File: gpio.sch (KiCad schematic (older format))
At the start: 1 part, among them U1 LFE5U-85F-6BG381C

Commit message: GPDI routed
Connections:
- net LTDC_TO_FPGA_B5: now also U1.B3 (PL14D); no longer U1.E5 (PL20C)
- net LTDC_TO_FPGA_B6: now also U1.F5 (PL20D); no longer U1.B2 (VREF1_7)
- net LTDC_TO_FPGA_B7: now also U1.E5 (PL20C); no longer U1.C2 (PL35D)
- net LTDC_TO_FPGA_G2: now also U1.B2 (VREF1_7); no longer U1.B3 (PL14D)
- net LTDC_TO_FPGA_R6: now also U1.C2 (PL35D); no longer U1.F5 (PL20D)
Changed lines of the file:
@@
 Text GLabel 4200 4000 0    60   Input ~ 0
 LTDC_TO_FPGA_R5
-Text GLabel 5700 4200 2    60   Input ~ 0
+Text GLabel 5700 4400 2    60   Input ~ 0
 LTDC_TO_FPGA_R6
 Text GLabel 4200 4900 0    60   Input ~ 0
@@
 Text GLabel 5700 5000 2    60   Input ~ 0
 LTDC_TO_FPGA_G6
-Text GLabel 5700 4400 2    60   Input ~ 0
+Text GLabel 4200 4200 0    60   Input ~ 0
 LTDC_TO_FPGA_B7
-Text GLabel 4200 4400 0    60   Input ~ 0
+Text GLabel 5700 4200 2    60   Input ~ 0
 LTDC_TO_FPGA_B6
-Text GLabel 4200 4200 0    60   Input ~ 0
+Text GLabel 5700 3800 2    60   Input ~ 0
 LTDC_TO_FPGA_B5
 Text GLabel 4200 4300 0    60   Input ~ 0
@@
 Text GLabel 5700 4600 2    60   Input ~ 0
 LTDC_TO_FPGA_B3
-Text GLabel 5700 3800 2    60   Input ~ 0
+Text GLabel 4200 4400 0    60   Input ~ 0
 LTDC_TO_FPGA_G2
 Text GLabel 5700 4900 2    60   Input ~ 0

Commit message: Adding DIB_V2 connector for SERDES, change battery, initial power fixes power
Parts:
- added J1: Conn_02x08_Odd_Even, Connector_PinSocket_2.54mm:PinSocket_2x08_P2.54mm_Horizontal, symbol Connector_Generic:Conn_02x08_Odd_Even
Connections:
- net labels added: +1V1, +2V5, +3V3, GND, S_0_N, S_0_P, S_1_N, S_1_P, S_2_N, S_2_P, S_3_N, S_3_P, S_C_N, S_C_P
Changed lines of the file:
@@
 EESchema Schematic File Version 4
-EELAYER 30 0
+LIBS:ulx3s-cache
+EELAYER 29 0
 EELAYER END
 $Descr A4 11693 8268
@@
 Text GLabel 5700 2200 2    60   Input ~ 0
 LTDC_FROM_FPGA_R4
+$Comp
+L Connector_Generic:Conn_02x08_Odd_Even J1
+U 1 1 61FF604B
+P 8450 3700
+F 0 "J1" H 8500 3075 50  0000 C CNN
+F 1 "Conn_02x08_Odd_Even" H 8500 3166 50  0000 C CNN
+F 2 "Connector_PinSocket_2.54mm:PinSocket_2x08_P2.54mm_Horizontal" H 8450 3700 50  0001 C CNN
+F 3 "~" H 8450 3700 50  0001 C CNN
+	1    8450 3700
+	-1   0    0    1
+$EndComp
+Text GLabel 8150 3300 0    60   Input ~ 0
++3V3
+Text GLabel 8150 3400 0    60   Input ~ 0
++2V5
+Text GLabel 8150 3500 0    60   Input ~ 0
++1V1
+Text GLabel 8650 3300 2    60   Input ~ 0
+GND
+Text GLabel 8650 3400 2    60   Input ~ 0
+GND
+Text GLabel 8650 3500 2    60   Input ~ 0
+GND
+Text GLabel 8150 3800 0    60   Input ~ 0
+S_0_P
+Text GLabel 8150 3900 0    60   Input ~ 0
+S_0_N
+Text GLabel 8150 3600 0    60   Input ~ 0
+S_C_P
+Text GLabel 8150 3700 0    60   Input ~ 0
+S_C_N
+Text GLabel 8150 4000 0    60   Input ~ 0
+S_1_P
+Text GLabel 8650 4000 2    60   Input ~ 0
+S_1_N
+Text GLabel 8650 3600 2    60   Input ~ 0
+S_2_P
+Text GLabel 8650 3700 2    60   Input ~ 0
+S_2_N
+Text GLabel 8650 3800 2    60   Input ~ 0
+S_3_P
+Text GLabel 8650 3900 2    60   Input ~ 0
+S_3_N
 $EndSCHEMATC

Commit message: Routing long signals
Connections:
- net labels added: SPI2_TO_FPGA_CLK, SPI2_TO_FPGA_CSB, SPI2_TO_FPGA_IRQ
- net labels removed: FREE10, FREE5, FREE_LEFT_10, SPI5_FROM_FPGA_CLK
- no-connect marks 22 -> 19
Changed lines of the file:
@@
 Text GLabel 4200 1900 0    50   BiDi ~ 0
 SPI4_TO_FPGA_CLK
-Text GLabel 4200 3900 0    60   Input ~ 0
-FREE_LEFT_10
-Text GLabel 5700 5100 2    60   Input ~ 0
-FREE10
 Text GLabel 5700 4100 2    60   Input ~ 0
 FREE8
-Text GLabel 5700 3900 2    60   Input ~ 0
-FREE5
 Text GLabel 5700 3600 2    60   Input ~ 0
 FREE6
-Text GLabel 5700 2000 2    50   BiDi ~ 0
-SPI5_FROM_FPGA_CLK
 Text GLabel 5700 1900 2    50   BiDi ~ 0
 SPI4_FROM_FPGA_CLK
@@
 NoConn ~ 5700 2300
 NoConn ~ 5700 2100
-NoConn ~ 4200 3900
-NoConn ~ 5700 5100
 NoConn ~ 5700 4100
-NoConn ~ 5700 3900
 NoConn ~ 5700 3600
 Text GLabel 5700 2200 2    60   Input ~ 0
@@
 Text GLabel 8650 3900 2    60   Input ~ 0
 S_3_N
+Text GLabel 5700 5100 2    50   BiDi ~ 0
+SPI2_TO_FPGA_CLK
+Text GLabel 5700 3900 2    50   BiDi ~ 0
+SPI2_TO_FPGA_IRQ
+Text GLabel 4200 3900 0    50   BiDi ~ 0
+SPI2_TO_FPGA_CSB
 $EndSCHEMATC

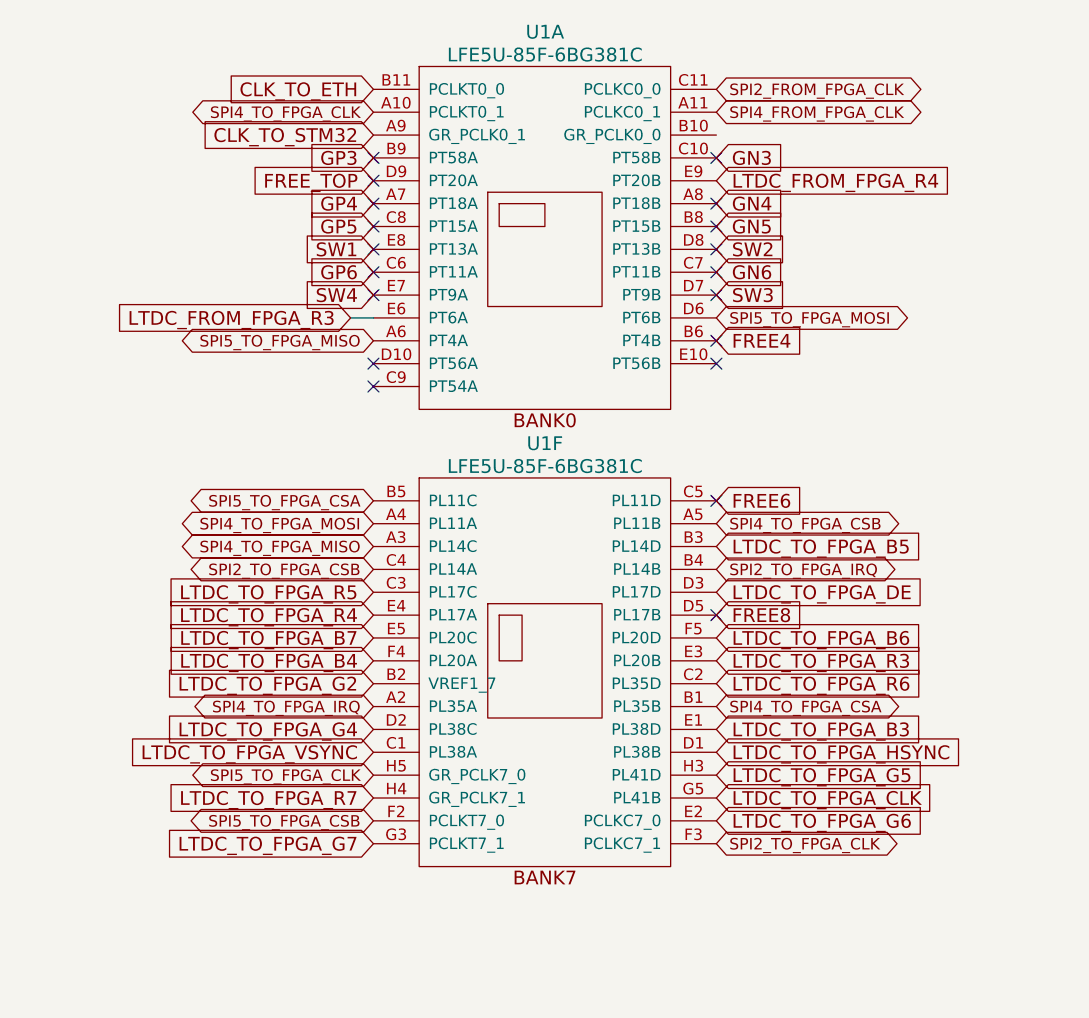
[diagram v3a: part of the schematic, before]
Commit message: Finish routing - removing CE and OpenHW number
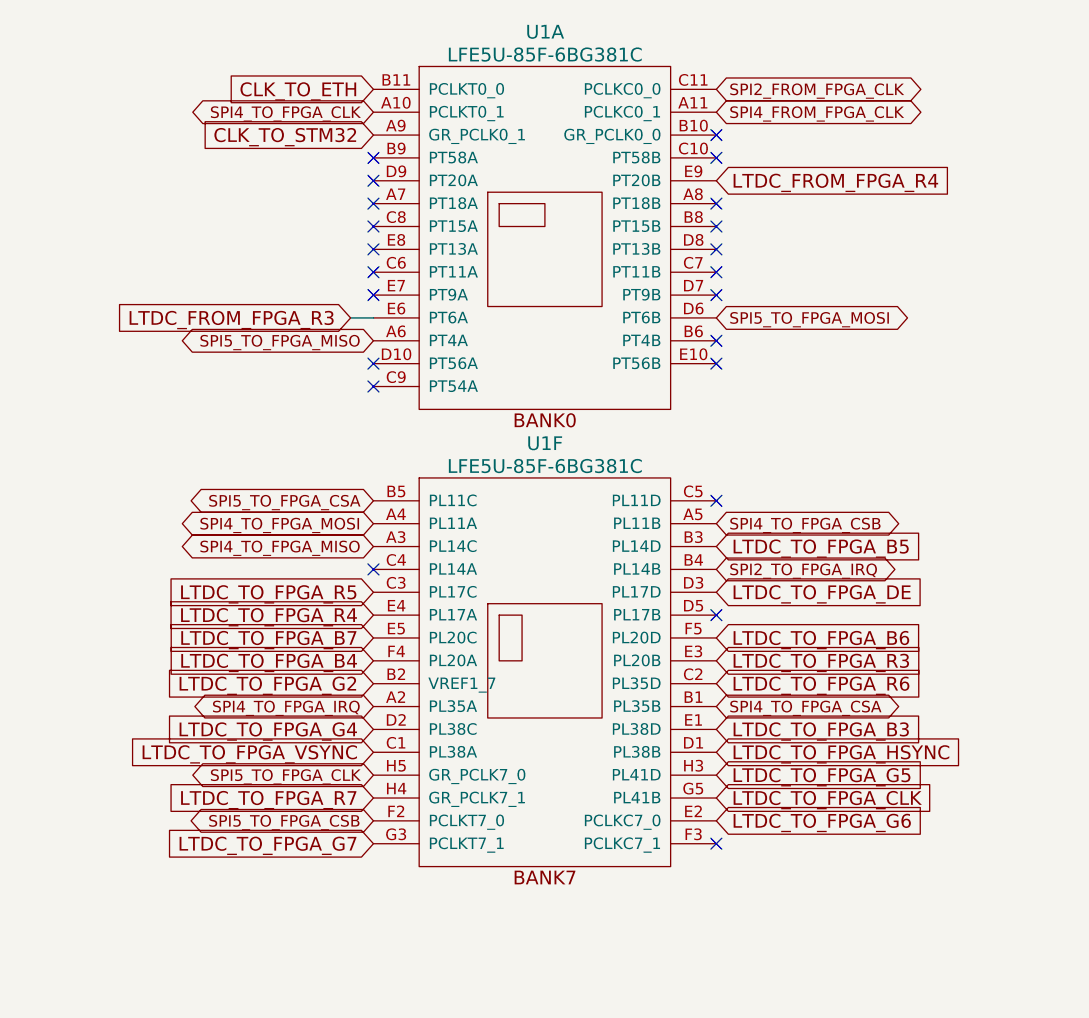
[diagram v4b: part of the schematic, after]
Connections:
- net labels removed: FREE4, FREE6, FREE8, FREE_TOP, GN3, GN4, GN5, GN6, GP3, GP4, GP5, GP6, SPI2_TO_FPGA_CLK, SPI2_TO_FPGA_CSB, SW1, SW2, SW3, SW4
- no-connect marks 19 -> 22
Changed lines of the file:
@@
 Comment4 ""
 $EndDescr
-Text GLabel 5700 2600 2    60   Input ~ 0
-GN6
-Text GLabel 4200 2600 0    60   Input ~ 0
-GP6
-Text GLabel 5700 2300 2    60   Input ~ 0
-GN4
 Text GLabel 4200 1800 0    60   Input ~ 0
 CLK_TO_ETH
 Text GLabel 4200 2000 0    60   Input ~ 0
 CLK_TO_STM32
-Text GLabel 4200 2300 0    60   Input ~ 0
-GP4
-Text GLabel 4200 2400 0    60   Input ~ 0
-GP5
-Text GLabel 5700 2400 2    60   Input ~ 0
-GN5
-Text GLabel 5700 2100 2    60   Input ~ 0
-GN3
-Text GLabel 4200 2100 0    60   Input ~ 0
-GP3
 Text Notes 950  7550 0    60   ~ 0
 GPIO route only A/B pairs as those are differential bidirectional\ndon't route C/D pairs to GPIO as those can be differential input only\nBANK0,1 are single-ended (non-differential)
-Text GLabel 4200 2500 0    60   Input ~ 0
-SW1
-Text GLabel 5700 2500 2    60   Input ~ 0
-SW2
-Text GLabel 5700 2700 2    60   Input ~ 0
-SW3
-Text GLabel 4200 2700 0    60   Input ~ 0
-SW4
 $Comp
 L lfe5bg381:LFE5UM-85F-6BG381C U1
@@
 Wire Wire Line
 	4100 2800 4200 2800
-Text GLabel 5700 2900 2    60   Input ~ 0
-FREE4
 Text GLabel 5700 3700 2    50   BiDi ~ 0
 SPI4_TO_FPGA_CSB
@@
 Text GLabel 4200 4500 0    50   BiDi ~ 0
 SPI4_TO_FPGA_IRQ
-Text GLabel 4200 2200 0    60   Input ~ 0
-FREE_TOP
 Text GLabel 4200 5100 0    60   Input ~ 0
 LTDC_TO_FPGA_G7
 Text GLabel 4200 1900 0    50   BiDi ~ 0
 SPI4_TO_FPGA_CLK
-Text GLabel 5700 4100 2    60   Input ~ 0
-FREE8
-Text GLabel 5700 3600 2    60   Input ~ 0
-FREE6
 Text GLabel 5700 1900 2    50   BiDi ~ 0
 SPI4_FROM_FPGA_CLK
@@
 Text GLabel 8650 3900 2    60   Input ~ 0
 S_3_N
-Text GLabel 5700 5100 2    50   BiDi ~ 0
-SPI2_TO_FPGA_CLK
 Text GLabel 5700 3900 2    50   BiDi ~ 0
 SPI2_TO_FPGA_IRQ
-Text GLabel 4200 3900 0    50   BiDi ~ 0
-SPI2_TO_FPGA_CSB
+NoConn ~ 5700 2000
+NoConn ~ 4200 3900
+NoConn ~ 5700 5100
 $EndSCHEMATC

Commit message: Routing SERDES
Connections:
- net labels added: SRCLKN, SRCLKP, SRXN00, SRXN01, SRXN10, SRXP00, SRXP01, SRXP10, STXN11, STXP11
- net labels removed: S_0_N, S_0_P, S_1_N, S_1_P, S_2_N, S_2_P, S_3_N, S_3_P, S_C_N, S_C_P
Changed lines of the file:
@@
 Text GLabel 8650 3500 2    60   Input ~ 0
 GND
-Text GLabel 8150 3800 0    60   Input ~ 0
-S_0_P
-Text GLabel 8150 3900 0    60   Input ~ 0
-S_0_N
-Text GLabel 8150 3600 0    60   Input ~ 0
-S_C_P
-Text GLabel 8150 3700 0    60   Input ~ 0
-S_C_N
-Text GLabel 8150 4000 0    60   Input ~ 0
-S_1_P
-Text GLabel 8650 4000 2    60   Input ~ 0
-S_1_N
-Text GLabel 8650 3600 2    60   Input ~ 0
-S_2_P
-Text GLabel 8650 3700 2    60   Input ~ 0
-S_2_N
-Text GLabel 8650 3800 2    60   Input ~ 0
-S_3_P
-Text GLabel 8650 3900 2    60   Input ~ 0
-S_3_N
 Text GLabel 5700 3900 2    50   BiDi ~ 0
 SPI2_TO_FPGA_IRQ
@@
 NoConn ~ 4200 3900
 NoConn ~ 5700 5100
+Text GLabel 8150 3900 0    60   Input ~ 0
+SRXN01
+Text GLabel 8650 3700 2    60   Input ~ 0
+SRXP10
+Text GLabel 8650 3600 2    60   Input ~ 0
+STXP11
+Text GLabel 8650 4000 2    60   Input ~ 0
+SRXP00
+Text GLabel 8650 3800 2    60   Input ~ 0
+SRCLKP
+Text GLabel 8150 3800 0    60   Input ~ 0
+SRCLKN
+Text GLabel 8150 4000 0    60   Input ~ 0
+SRXN00
+Text GLabel 8150 3600 0    60   Input ~ 0
+STXN11
+Text GLabel 8150 3700 0    60   Input ~ 0
+SRXN10
+Text GLabel 8650 3900 2    60   Input ~ 0
+SRXP01
 $EndSCHEMATC
